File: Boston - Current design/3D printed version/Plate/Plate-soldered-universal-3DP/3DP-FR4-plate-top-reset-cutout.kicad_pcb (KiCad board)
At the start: 2 copper layers, 396 x 161 mm, 31 parts

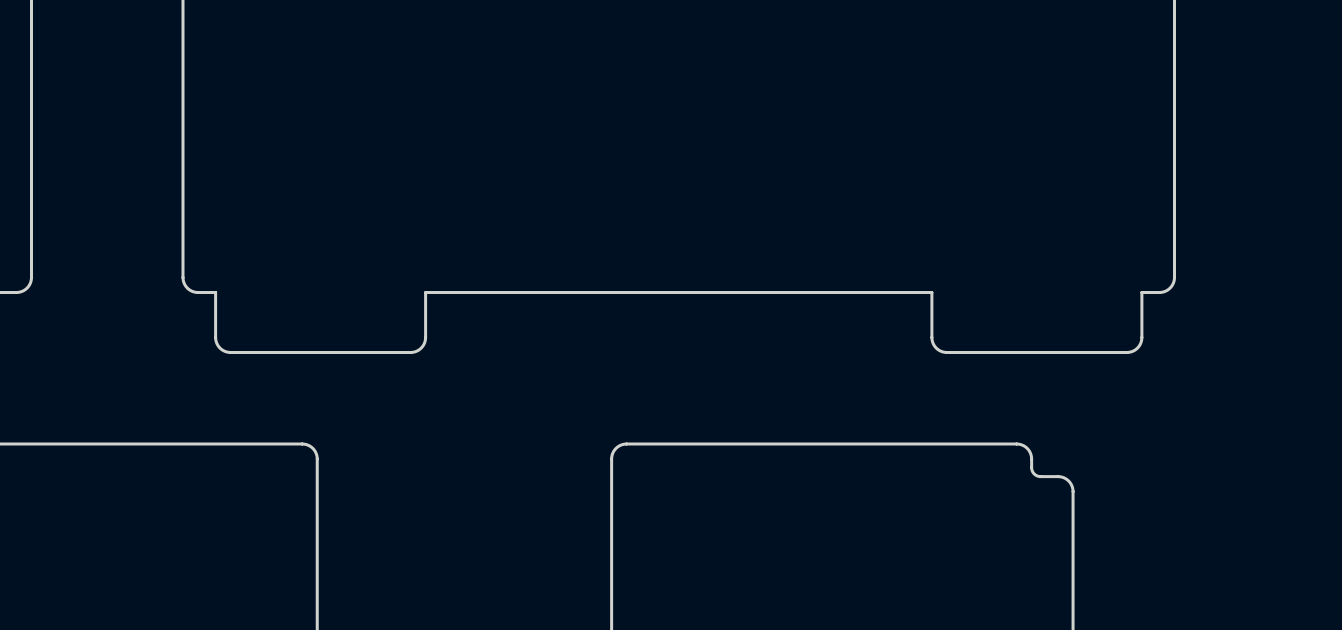
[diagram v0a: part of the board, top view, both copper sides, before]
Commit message: Rounded off sharp corners
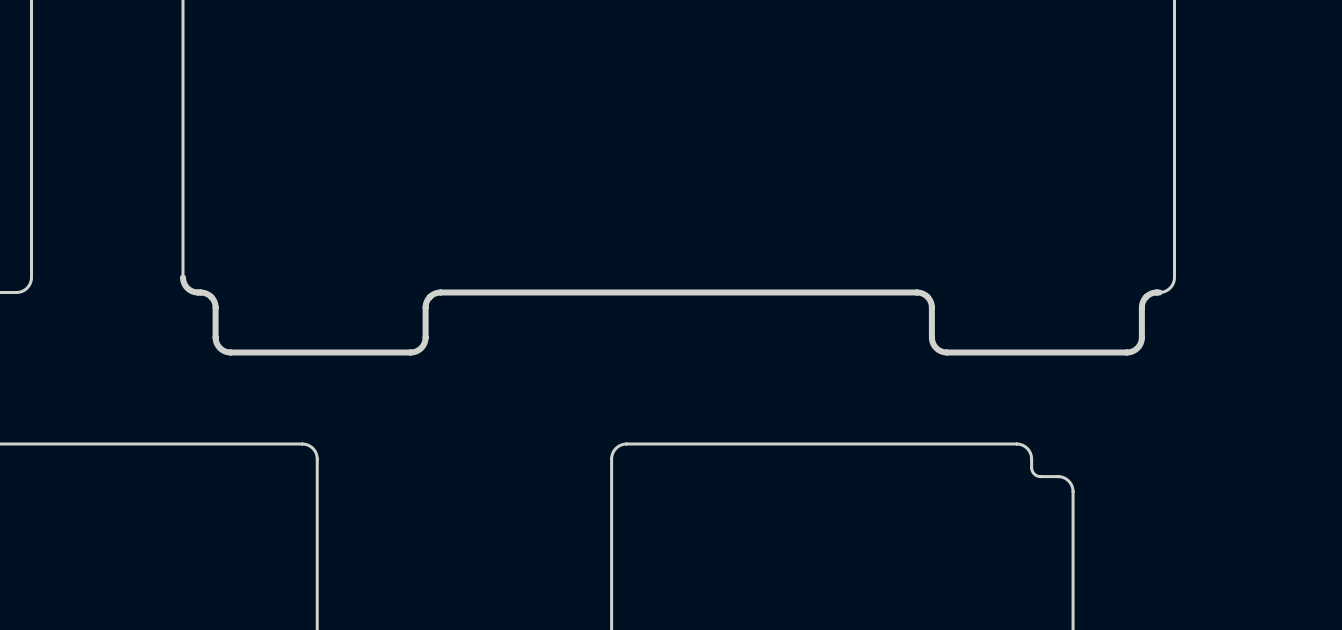
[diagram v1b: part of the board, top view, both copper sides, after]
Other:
- outline, holes or cut-outs redrawn
- board text added: "Boston 3DP Soldered plate - universal V0.7 - June 29, 2023"
- board text removed: "Plate V0.5 - May 15, 2022"
- board text removed: "Soldered plate - universal March 25, 2023"
